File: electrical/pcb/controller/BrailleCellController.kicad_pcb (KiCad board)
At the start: 2 copper layers, 7 x 12 mm, 3 parts, among them J1 Conn_01x08_Socket, J2 Conn_01x08_Socket, U1 HV509K6-G

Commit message: Power System
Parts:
- moved J1 1.25 mm to (203.5, 61.0)
- moved J2 1.25 mm to (203.5, 59.0)
- moved U1 1.25 mm to (203.5, 55.0)
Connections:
- U1 pad 14: unconnected-(U1-VPP-Pad14) -> +215V
- U1 pad 17: unconnected-(U1-DIN-Pad17) -> /DIN
- U1 pad 19: unconnected-(U1-CLK-Pad19) -> /CLK
- U1 pad 20: unconnected-(U1-VDD-Pad20) -> +3.3VP
- U1 pad 21: unconnected-(U1-*POL-Pad21) -> /LE
- U1 pad 22: unconnected-(U1-*LE-Pad22) -> /LE
- U1 pad 24: unconnected-(U1-DOUT-Pad24) -> /DOUT
- U1 pad 26: unconnected-(U1-VBIAS-Pad26) -> +3.3VP
- U1 pad 27: unconnected-(U1-HVGND-Pad27) -> GND
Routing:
- net GND: track 0.00 -> 5.74 mm
- net (no net): vias 4 -> 0
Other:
- outline, holes or cut-outs redrawn

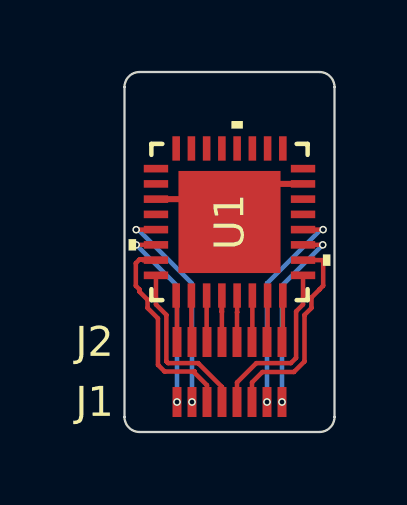
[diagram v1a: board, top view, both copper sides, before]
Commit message: cell shifter routed
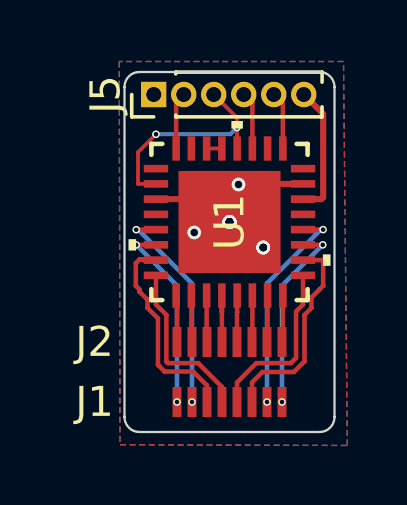
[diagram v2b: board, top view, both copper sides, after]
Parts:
- added J5: Conn_01x05_Socket, Connector_PinHeader_1.00mm:PinHeader_1x06_P1.00mm_Vertical, F.Cu at (201.0, 50.8)
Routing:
- net +3.3VP: track 0.00 -> 7.42 mm, vias 0 -> 2
- net +215V: track 0.00 -> 4.39 mm
- net /DIN: track 0.00 -> 1.92 mm
- net /CLK: track 0.00 -> 1.92 mm
- net /DOUT: track 0.00 -> 1.90 mm
- net /LE: track 0.00 -> 0.51 mm
- net GND: vias 0 -> 10
- added copper zone on B.Cu, net GND
- added copper zone on F.Cu, net GND
